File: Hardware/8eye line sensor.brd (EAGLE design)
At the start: 106.7 x 27.9 mm, 82 parts, among them U1 SX1509, U101 QRE1113, U102 QRE1113, U103 QRE1113, U104 QRE1113, U105 QRE1113, U106 QRE1113, U107 QRE1113, U108 QRE1113, U2 74AC125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

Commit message: Fixed github/qc finds
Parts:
- removed STANDOFF8: STAND-OFF, SparkFun-Electromechanical:STAND-OFF
- added STANDOFF2: STAND-OFF, SparkFun-Electromechanical:STAND-OFF
- R10, R12, R14, R22, R26, R27, R28, R4: value 68K -> 68.1k; device SparkFun-Resistors:0603 -> SparkFun-Resistors:0603-RES
- R2: value 33OHM -> 330; device SparkFun-Resistors:0603 -> SparkFun-Resistors:0603-RES
- moved STANDOFF6 24.0 mm to (72.4, 2.54), turned to 90 degrees
- moved STANDOFF4 7.78 mm to (58.3, 2.54), turned to 90 degrees
- moved STANDOFF5 7.78 mm to (66.0, 2.54), turned to 90 degrees
- moved STANDOFF3 7.78 mm to (48.4, 2.54), turned to 90 degrees
- turned STANDOFF1 to 90 degrees
- renumbered LED2 to D9, STANDOFF7 to STANDOFF1

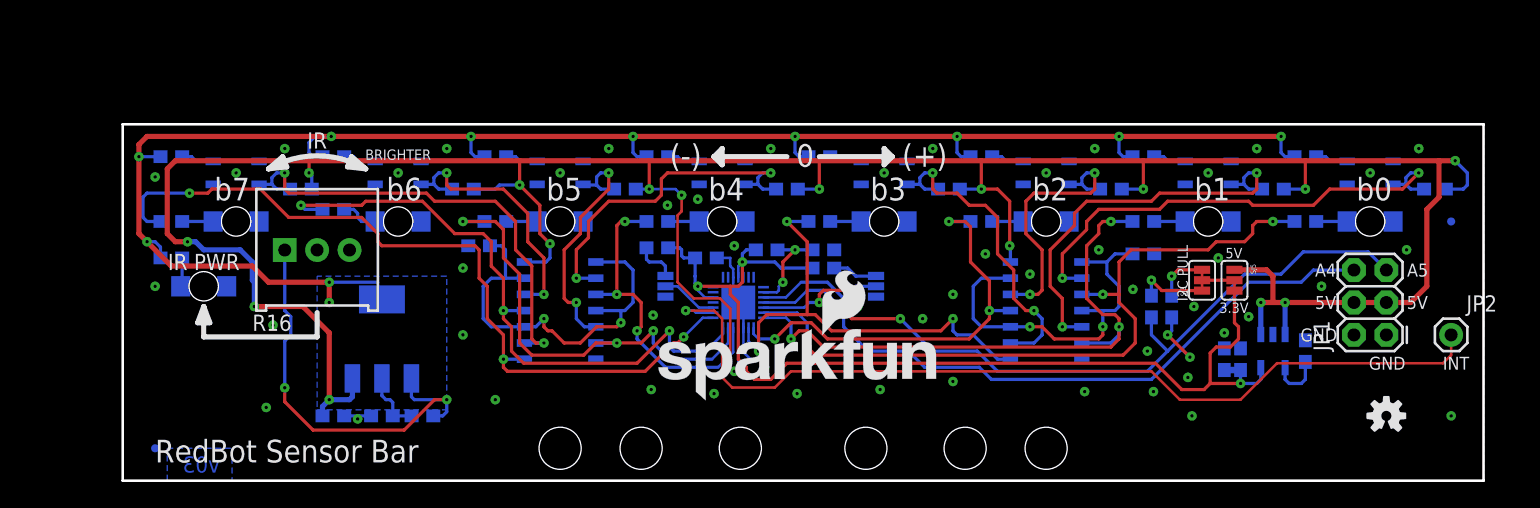
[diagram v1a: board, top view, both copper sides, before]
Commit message: v04: IR LED power ctrl, regulated receiver supply
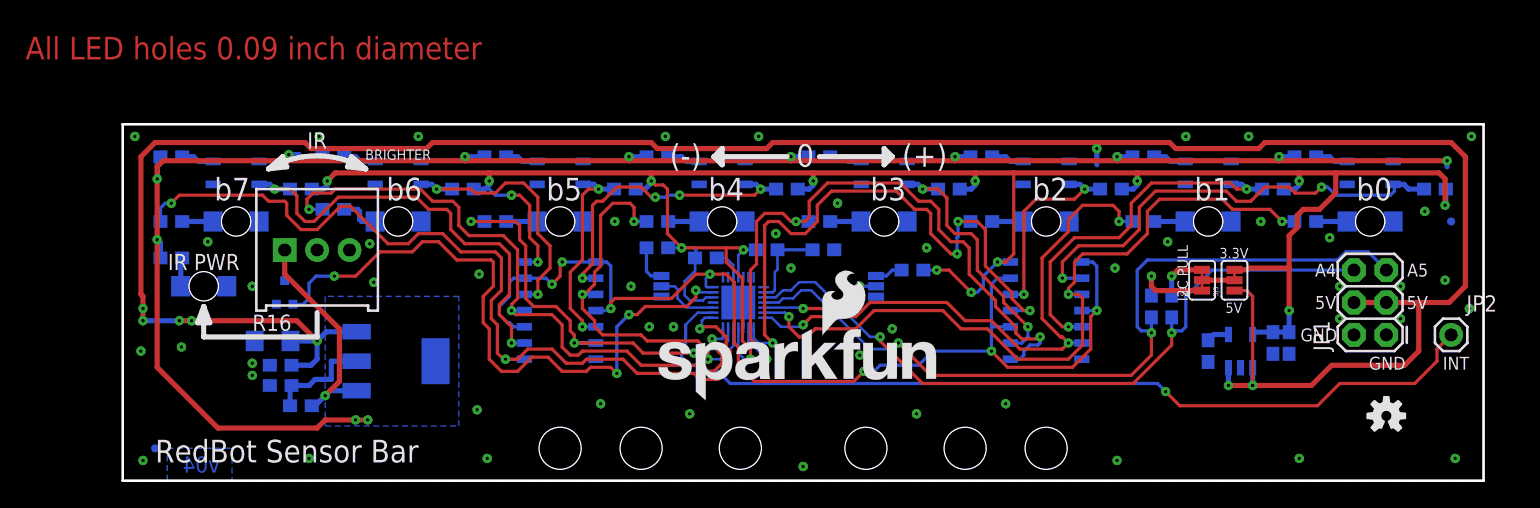
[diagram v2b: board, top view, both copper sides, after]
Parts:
- removed R15, R29: 10K, SparkFun-Resistors:0603-RES
- added C8: 10uF, SparkFun-Capacitors:EIA3216
- added Q1: MOSFET-NCHANNEL2N7002PW, SparkFun-DiscreteSemi:SOT323
- moved R1 9.56 mm to (14.0, 5.87)
- moved C1 8.29 mm to (12.4, 7.46)
- moved C5 7.62 mm to (85.1, 10.2), turned to 270 degrees
- moved R33 6.99 mm to (61.9, 16.5), turned to 0 degrees
- moved C2 5.73 mm to (12.4, 9.05), turned to 0 degrees
- moved C7 5.24 mm to (91.4, 10.8), turned to 270 degrees
- moved C4 2.84 mm to (90.2, 10.8), turned to 270 degrees
- moved U3 2.54 mm to (87.6, 10.2), turned to 0 degrees
- moved U5 2.07 mm to (21.4, 9.37), turned to 90 degrees
- moved SJ2 0.32 mm to (42.2, 15.2)
- turned SJ5 to 90 degrees
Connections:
- removed net !ENBLSB: R15.2, U2.1, U2.10, U2.13, U2.4
- removed net !ENBMSB: R29.2, U6.1, U6.10, U6.13, U6.4
- new net !FBLEDEN: U1.14, U2.1, U2.10, U2.13, U2.4, U6.1, U6.10, U6.13, U6.4
- new net !IRLEDEN: Q1.1, U1.13
- net GND: now also C8.C, Q1.2; no longer R15.1, R29.1
- net I2C_PWR: now also R10.2, R12.2, R14.2, R22.2, R26.2, R27.2, R28.2, R4.2, U1.4, U2.14, U6.14
- net N$1: now also Q1.3
- net VCC: now also C8.A; no longer R10.2, R12.2, R14.2, R22.2, R26.2, R27.2, R28.2, R4.2, U1.4, U2.14, U6.14
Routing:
- net I2C_PWR: track 82.6 -> 191.5 mm, vias 3 -> 17
- net !FBLEDEN: track 0.00 -> 87.0 mm, vias 0 -> 7
- net !IRLEDEN: track 0.00 -> 51.7 mm, vias 0 -> 4
- net VCC: track 238.9 -> 197.3 mm, vias 17 -> 8
- net !ENBMSB: track 32.6 -> 0.00 mm, vias 2 -> 0
- net !ENBLSB: track 29.7 -> 0.00 mm, vias 2 -> 0
- net SEN3BUF: track 36.8 -> 51.6 mm
- net SEN2BUF: track 33.9 -> 48.2 mm, vias 3 -> 4
- net LED_BIAS: track 147.6 -> 161.0 mm, vias 11 -> 12
- net N$1: track 33.3 -> 20.0 mm, vias 2 -> 1
- net SEN7BUF: track 62.0 -> 69.7 mm
- net SEN2: track 21.5 -> 15.6 mm
- net GND: track 12.0 -> 6.76 mm, vias 52 -> 50
- net SEN4BUF: track 25.5 -> 30.3 mm
- net SEN3: track 25.3 -> 20.6 mm
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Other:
- board text added: "All LED holes 0.09 inch diameter"
- board text added: "Dimensions from origin"
- board text added: "v04"
- board text removed: "Dimentions from origin"
- board text removed: "v03"

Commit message: Fixed QC issues
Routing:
- net LED_BIAS: track 161.0 -> 147.2 mm, vias 12 -> 11
- net N$6: track 1.78 -> 3.76 mm
- net VCC: track 197.3 -> 195.6 mm, vias 8 -> 7
- net !FBLEDEN: track 87.0 -> 88.0 mm
- net !IRLEDEN: track 51.7 -> 50.8 mm
- net SEN7BUF: track 69.7 -> 69.1 mm

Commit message: V_1.0 update
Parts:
- R30, R32: value 10K -> 4.7K
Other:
- board text added: "A5/SCL"
- board text added: "SDA/A4"
- board text removed: "00"
- board text removed: "01"
- board text removed: "10"
- board text removed: "11"
- board text removed: "A4"
- board text removed: "A5"
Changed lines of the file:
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@@
 <setting verticaltext="up"/>
 </settings>
-<grid distance="0.1" unitdist="inch" unit="inch" style="lines" multiple="1" display="yes" altdistance="0.003125" altunitdist="inch" altunit="inch"/>
+<grid distance="0.1" unitdist="inch" unit="inch" style="lines" multiple="1" display="yes" altdistance="0.005" altunitdist="inch" altunit="inch"/>
 <layers>
 <layer number="1" name="Top" color="4" fill="1" visible="yes" active="yes"/>
@@
 <text x="34.6075" y="22.86" size="1.778" layer="21" font="vector" ratio="15" align="center">b5</text>
 <text x="6.35" y="16.51" size="1.27" layer="21" font="vector" ratio="15" align="bottom-center">IR PWR</text>
-<text x="94.2975" y="16.51" size="1.016" layer="21" font="vector" ratio="15" align="center">A4</text>
-<text x="101.5111" y="16.51" size="1.016" layer="21" font="vector" ratio="15" align="center">A5</text>
+<text x="95.1865" y="16.51" size="1.016" layer="21" font="vector" ratio="15" align="center-right">SDA/A4</text>
+<text x="100.6221" y="16.51" size="1.016" layer="21" font="vector" ratio="15" align="center-left">A5/SCL</text>
 <text x="93.7641" y="11.43" size="1.016" layer="21" font="vector" ratio="15" align="center">GND</text>
 <text x="101.4857" y="13.97" size="1.016" layer="21" font="vector" ratio="15" align="center">5V</text>
@@
 <text x="86.4489" y="13.15085" size="0.8128" layer="21" font="vector" ratio="15">5V</text>
 <text x="85.97265" y="17.4371" size="0.8128" layer="21" font="vector" ratio="15">3.3V</text>
-<text x="96.52" y="6.731" size="0.9144" layer="22" font="vector" ratio="15" rot="MR180" align="bottom-center">00</text>
-<text x="96.52" y="5.588" size="0.9144" layer="22" font="vector" ratio="15" rot="MR180" align="bottom-center">01</text>
-<text x="96.52" y="4.445" size="0.9144" layer="22" font="vector" ratio="15" rot="MR180" align="bottom-center">10</text>
-<text x="96.52" y="3.302" size="0.9144" layer="22" font="vector" ratio="15" rot="MR180" align="bottom-center">11</text>
+<text x="96.647" y="6.731" size="0.9144" layer="22" font="vector" ratio="15" rot="MR180" align="bottom-center">0</text>
+<text x="96.647" y="5.588" size="0.9144" layer="22" font="vector" ratio="15" rot="MR180" align="bottom-center">1</text>
+<text x="96.647" y="4.445" size="0.9144" layer="22" font="vector" ratio="15" rot="MR180" align="bottom-center">0</text>
+<text x="96.647" y="3.302" size="0.9144" layer="22" font="vector" ratio="15" rot="MR180" align="bottom-center">1</text>
 <text x="99.568" y="6.731" size="0.9144" layer="22" font="vector" ratio="15" rot="MR180" align="bottom-center">0x3E</text>
 <text x="99.568" y="5.588" size="0.9144" layer="22" font="vector" ratio="15" rot="MR180" align="bottom-center">0x3F</text>
@@
 <circle x="15.875" y="6.6675" radius="0.508246875" width="0.4064" layer="29"/>
 <circle x="15.875" y="6.6675" radius="0.1774875" width="0.4064" layer="29"/>
+<text x="94.488" y="6.731" size="0.9144" layer="22" font="vector" ratio="15" rot="MR180" align="bottom-center">0</text>
+<text x="94.488" y="5.588" size="0.9144" layer="22" font="vector" ratio="15" rot="MR180" align="bottom-center">0</text>
+<text x="94.488" y="4.445" size="0.9144" layer="22" font="vector" ratio="15" rot="MR180" align="bottom-center">1</text>
+<text x="94.488" y="3.302" size="0.9144" layer="22" font="vector" ratio="15" rot="MR180" align="bottom-center">1</text>
+<wire x1="93.472" y1="7.239" x2="95.631" y2="7.239" width="0.254" layer="22"/>
+<wire x1="93.472" y1="2.032" x2="95.631" y2="2.032" width="0.254" layer="22"/>
+<wire x1="93.472" y1="2.032" x2="93.472" y2="7.239" width="0.254" layer="22"/>
+<text x="96.647" y="7.46125" size="0.8128" layer="22" font="vector" ratio="15" rot="MR0" align="bottom-center">A0</text>
+<text x="94.4499" y="7.5057" size="0.8128" layer="22" font="vector" ratio="15" rot="MR0" align="bottom-center">A1</text>
 </plain>
 <attributes>
@@
 <attribute name="VALUE" value="100" x="92.71" y="25.4" size="1.778" layer="28" rot="MR180" display="off"/>
 </element>
-<element name="R30" library="SparkFun-Resistors" package="0603-RES" value="10K" x="80.645" y="13.6525" rot="MR90">
-<attribute name="PROD_ID" value="RES-00824" x="80.645" y="13.6525" size="1.778" layer="28" rot="MR90" display="off"/>
-<attribute name="VALUE" value="10K" x="80.645" y="13.6525" size="1.778" layer="28" rot="MR90" display="off"/>
-</element>
-<element name="R32" library="SparkFun-Resistors" package="0603-RES" value="10K" x="82.2325" y="13.6525" rot="MR90">
-<attribute name="PROD_ID" value="RES-00824" x="82.2325" y="13.6525" size="1.778" layer="28" rot="MR90" display="off"/>
-<attribute name="VALUE" value="10K" x="82.2325" y="13.6525" size="1.778" layer="28" rot="MR90" display="off"/>
+<element name="R30" library="SparkFun-Resistors" package="0603-RES" value="4.7K" x="80.645" y="13.6525" rot="MR90">
+<attribute name="PROD_ID" value="RES-07857" x="80.645" y="13.6525" size="1.778" layer="28" rot="MR90" display="off"/>
+<attribute name="VALUE" value="4.7K" x="80.645" y="13.6525" size="1.778" layer="28" rot="MR90" display="off"/>
+</element>
+<element name="R32" library="SparkFun-Resistors" package="0603-RES" value="4.7K" x="82.2325" y="13.6525" rot="MR90">
+<attribute name="PROD_ID" value="RES-07857" x="82.2325" y="13.6525" size="1.778" layer="28" rot="MR90" display="off"/>
+<attribute name="VALUE" value="4.7K" x="82.2325" y="13.6525" size="1.778" layer="28" rot="MR90" display="off"/>
 </element>
 <element name="R4" library="SparkFun-Resistors" package="0603-RES" value="68.1k" x="102.87" y="22.86" rot="MR180">

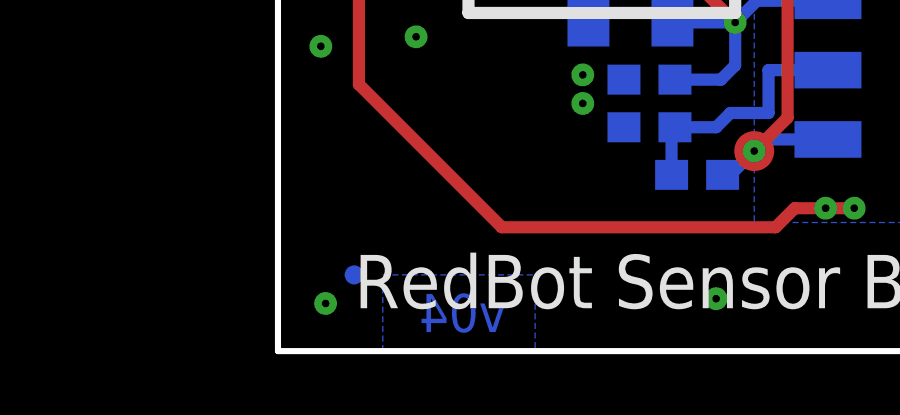
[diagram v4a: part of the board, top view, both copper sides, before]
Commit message: Fixed rev number and readme
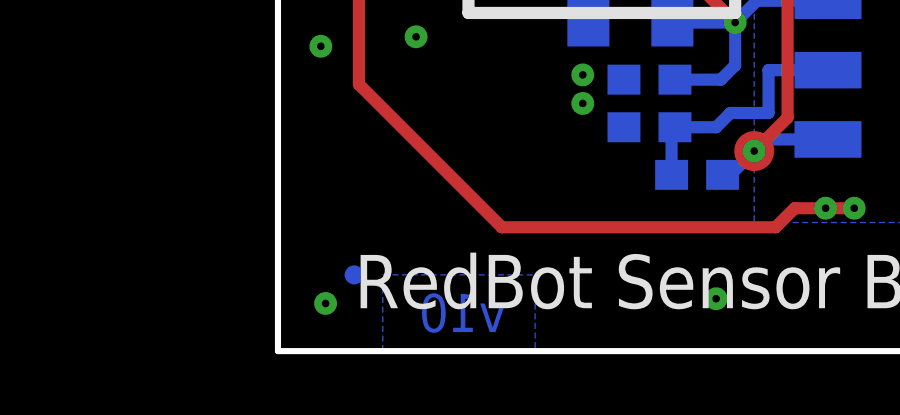
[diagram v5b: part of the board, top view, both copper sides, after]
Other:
- board text added: "v10"
- board text removed: "v04"
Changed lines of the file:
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@@
 <text x="99.1235" y="9.2075" size="1.016" layer="21" font="vector" ratio="15" rot="R180" align="center">GND</text>
 <text x="104.521" y="9.2075" size="1.016" layer="21" font="vector" ratio="15" rot="R180" align="center">INT</text>
-<text x="7.62" y="1.27" size="1.27" layer="16" font="vector" ratio="15" rot="MR180" align="center-right">v04</text>
+<text x="7.62" y="1.27" size="1.27" layer="16" font="vector" ratio="15" rot="MR180" align="center-right">v10</text>
 <text x="82.68335" y="18.48485" size="0.8128" layer="21" font="vector" ratio="15" rot="R270">I2C PULL</text>
 <text x="60.29325" y="15.24" size="0.8128" layer="22" font="vector" ratio="15" rot="MR90" align="bottom-center">A0</text>
